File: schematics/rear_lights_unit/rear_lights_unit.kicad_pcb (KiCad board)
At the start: 2 copper layers, 0 parts

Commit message: rear light unit: finished first draft of PCB, regenerated all related files
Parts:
- added BT1: Battery_Cell, FarrhadTech:BatteryHolder_18650, B.Cu at (138.3, 110.5)
- added C1: 0.01uF, Capacitor_THT:C_Rect_L4.6mm_W2.0mm_P2.50mm_MKS02_FKP02, B.Cu at (61.6, 117.9)
- added C2: 10uF, Capacitor_THT:C_Rect_L4.6mm_W2.0mm_P2.50mm_MKS02_FKP02, B.Cu at (72.9, 102.1)
- added C3: 0.01uF, Capacitor_THT:C_Rect_L4.6mm_W2.0mm_P2.50mm_MKS02_FKP02, B.Cu at (94.6, 117.9)
- added C4: 10uF, Capacitor_THT:C_Rect_L4.6mm_W2.0mm_P2.50mm_MKS02_FKP02, B.Cu at (105.9, 102.1)
- added C5: 10uF, Capacitor_THT:CP_Radial_D5.0mm_P2.00mm, B.Cu at (54.6, 96.8)
- added D1: LED, LED_THT:LED_D5.0mm, F.Cu at (104.6, 59.9)
- added D10: LED, LED_THT:LED_D5.0mm, F.Cu at (162.1, 68.1)
- added D11: LED, LED_THT:LED_D5.0mm, F.Cu at (162.1, 76.2)
- added D12: LED, LED_THT:LED_D5.0mm, F.Cu at (162.1, 84.3)
- added D13: LED, LED_THT:LED_D5.0mm, F.Cu at (178.3, 62.2)
- added D14: LED, LED_THT:LED_D5.0mm, F.Cu at (178.3, 71.4)
- added D15: LED, LED_THT:LED_D5.0mm, F.Cu at (178.3, 80.5)
- added D16: LED, LED_THT:LED_D5.0mm, F.Cu at (199.6, 66.8)
- added D17: LED, LED_THT:LED_D5.0mm, F.Cu at (129.0, 60.2)
- added D18: LED, LED_THT:LED_D5.0mm, F.Cu at (129.0, 68.3)
- added D19: LED, LED_THT:LED_D5.0mm, F.Cu at (129.0, 76.5)
- added D2: LED, LED_THT:LED_D5.0mm, F.Cu at (104.6, 68.1)
- added D20: LED, LED_THT:LED_D5.0mm, F.Cu at (129.0, 84.6)
- added D21: LED, LED_THT:LED_D5.0mm, F.Cu at (138.2, 60.2)
- added D22: LED, LED_THT:LED_D5.0mm, F.Cu at (138.2, 68.3)
- added D23: LED, LED_THT:LED_D5.0mm, F.Cu at (138.2, 76.5)
- added D24: LED, LED_THT:LED_D5.0mm, F.Cu at (138.2, 84.6)
- added D25: LED, LED_THT:LED_D5.0mm, F.Cu at (67.0, 77.5)
- added D26: LED, LED_THT:LED_D5.0mm, F.Cu at (199.6, 75.9)
- added D3: LED, LED_THT:LED_D5.0mm, F.Cu at (104.6, 76.2)
- added D4: LED, LED_THT:LED_D5.0mm, F.Cu at (104.6, 84.3)
- added D5: LED, LED_THT:LED_D5.0mm, F.Cu at (88.4, 63.8)
- added D6: LED, LED_THT:LED_D5.0mm, F.Cu at (88.4, 72.9)
- added D7: LED, LED_THT:LED_D5.0mm, F.Cu at (88.4, 82.0)
- added D8: LED, LED_THT:LED_D5.0mm, F.Cu at (67.0, 68.3)
- added D9: LED, LED_THT:LED_D5.0mm, F.Cu at (162.1, 59.9)
- added G***: LOGO, FarrhadTech:resisty_0.5x0.65inch, F.Cu at (155.2, 111.5)
- added J1: Conn_01x04_Socket, Connector_JST:JST_XH_S4B-XH-A_1x04_P2.50mm_Horizontal, B.Cu at (206.0, 84.6)
- added Q1: IRLZ44N, FarrhadTech:TO-220-3_Horizontal_TabUpNoHole, B.Cu at (80.3, 97.3)
- added Q2: IRLZ44N, FarrhadTech:TO-220-3_Horizontal_TabUpNoHole, B.Cu at (113.0, 97.3)
- added R1: 120, Resistor_THT:R_Axial_DIN0207_L6.3mm_D2.5mm_P10.16mm_Horizontal, B.Cu at (101.6, 59.9)
- added R10: 120, Resistor_THT:R_Axial_DIN0207_L6.3mm_D2.5mm_P10.16mm_Horizontal, B.Cu at (165.1, 68.1)
- added R11: 120, Resistor_THT:R_Axial_DIN0207_L6.3mm_D2.5mm_P10.16mm_Horizontal, B.Cu at (165.1, 76.2)
- added R12: 120, Resistor_THT:R_Axial_DIN0207_L6.3mm_D2.5mm_P10.16mm_Horizontal, B.Cu at (165.1, 84.3)
- added R13: 120, Resistor_THT:R_Axial_DIN0207_L6.3mm_D2.5mm_P10.16mm_Horizontal, B.Cu at (183.9, 62.2)
- added R14: 120, Resistor_THT:R_Axial_DIN0207_L6.3mm_D2.5mm_P10.16mm_Horizontal, B.Cu at (183.9, 71.4)
- added R15: 120, Resistor_THT:R_Axial_DIN0207_L6.3mm_D2.5mm_P10.16mm_Horizontal, B.Cu at (183.9, 80.5)
- added R16: 120, Resistor_THT:R_Axial_DIN0207_L6.3mm_D2.5mm_P10.16mm_Horizontal, B.Cu at (202.7, 66.8)
- added R17: 120, Resistor_THT:R_Axial_DIN0207_L6.3mm_D2.5mm_P10.16mm_Horizontal, B.Cu at (126.5, 60.2)
- added R18: 120, Resistor_THT:R_Axial_DIN0207_L6.3mm_D2.5mm_P10.16mm_Horizontal, B.Cu at (126.5, 68.3)
- added R19: 120, Resistor_THT:R_Axial_DIN0207_L6.3mm_D2.5mm_P10.16mm_Horizontal, B.Cu at (126.5, 76.5)
- added R2: 120, Resistor_THT:R_Axial_DIN0207_L6.3mm_D2.5mm_P10.16mm_Horizontal, B.Cu at (101.6, 68.1)
- added R20: 120, Resistor_THT:R_Axial_DIN0207_L6.3mm_D2.5mm_P10.16mm_Horizontal, B.Cu at (126.5, 84.6)
- added R21: 120, Resistor_THT:R_Axial_DIN0207_L6.3mm_D2.5mm_P10.16mm_Horizontal, B.Cu at (150.9, 60.2)
- added R22: 120, Resistor_THT:R_Axial_DIN0207_L6.3mm_D2.5mm_P10.16mm_Horizontal, B.Cu at (150.9, 68.3)
- added R23: 120, Resistor_THT:R_Axial_DIN0207_L6.3mm_D2.5mm_P10.16mm_Horizontal, B.Cu at (150.9, 76.5)
- added R24: 120, Resistor_THT:R_Axial_DIN0207_L6.3mm_D2.5mm_P10.16mm_Horizontal, B.Cu at (150.9, 84.6)
- added R25: 7.5k, Resistor_THT:R_Axial_DIN0207_L6.3mm_D2.5mm_P10.16mm_Horizontal, B.Cu at (72.0, 113.0)
- added R26: 75k, Resistor_THT:R_Axial_DIN0207_L6.3mm_D2.5mm_P10.16mm_Horizontal, B.Cu at (55.4, 113.5)
- added R27: 100, Resistor_THT:R_Axial_DIN0207_L6.3mm_D2.5mm_P10.16mm_Horizontal, B.Cu at (72.6, 108.2)
- added R28: 10k, Resistor_THT:R_Axial_DIN0207_L6.3mm_D2.5mm_P10.16mm_Horizontal, B.Cu at (72.0, 117.9)
- added R29: 7.5k, Resistor_THT:R_Axial_DIN0207_L6.3mm_D2.5mm_P10.16mm_Horizontal, B.Cu at (104.9, 113.0)
- added R3: 120, Resistor_THT:R_Axial_DIN0207_L6.3mm_D2.5mm_P10.16mm_Horizontal, B.Cu at (101.6, 76.2)
- added R30: 75k, Resistor_THT:R_Axial_DIN0207_L6.3mm_D2.5mm_P10.16mm_Horizontal, B.Cu at (88.3, 113.5)
- added R31: 10k, Resistor_THT:R_Axial_DIN0207_L6.3mm_D2.5mm_P10.16mm_Horizontal, B.Cu at (104.9, 117.9)
- added R32: 100, Resistor_THT:R_Axial_DIN0207_L6.3mm_D2.5mm_P10.16mm_Horizontal, B.Cu at (105.7, 108.2)
- added R33: 120, Resistor_THT:R_Axial_DIN0207_L6.3mm_D2.5mm_P10.16mm_Horizontal, B.Cu at (64.0, 77.5)
- added R34: 120, Resistor_THT:R_Axial_DIN0207_L6.3mm_D2.5mm_P10.16mm_Horizontal, B.Cu at (202.7, 75.9)
- added R4: 120, Resistor_THT:R_Axial_DIN0207_L6.3mm_D2.5mm_P10.16mm_Horizontal, B.Cu at (101.6, 84.3)
- added R5: 120, Resistor_THT:R_Axial_DIN0207_L6.3mm_D2.5mm_P10.16mm_Horizontal, B.Cu at (82.8, 63.8)
- added R6: 120, Resistor_THT:R_Axial_DIN0207_L6.3mm_D2.5mm_P10.16mm_Horizontal, B.Cu at (82.8, 72.9)
- added R7: 120, Resistor_THT:R_Axial_DIN0207_L6.3mm_D2.5mm_P10.16mm_Horizontal, B.Cu at (82.8, 82.0)
- added R8: 120, Resistor_THT:R_Axial_DIN0207_L6.3mm_D2.5mm_P10.16mm_Horizontal, B.Cu at (64.0, 68.3)
- added R9: 120, Resistor_THT:R_Axial_DIN0207_L6.3mm_D2.5mm_P10.16mm_Horizontal, B.Cu at (165.1, 59.9)
- added SW2: rocker_switch, Button_Switch_THT:SW_Lever_1P2T_NKK_GW12LxH, B.Cu at (197.9, 90.9)
- added TP1: VBATT, TestPoint:TestPoint_Keystone_5000-5004_Miniature, B.Cu at (184.7, 95.8)
- added TP2: GND, TestPoint:TestPoint_Keystone_5000-5004_Miniature, B.Cu at (168.9, 95.8)
- added TP3: LEFT, TestPoint:TestPoint_Keystone_5000-5004_Miniature, B.Cu at (179.3, 95.8)
- added TP4: RIGHT, TestPoint:TestPoint_Keystone_5000-5004_Miniature, B.Cu at (174.2, 95.8)
- added U1: LMC555xN, Package_DIP:DIP-8_W7.62mm, B.Cu at (66.5, 103.9)
- added U2: LMC555xN, Package_DIP:DIP-8_W7.62mm, B.Cu at (99.6, 103.9)
- added U3: TP4056 module, FarrhadTech:TP4065, B.Cu at (126.8, 104.9)
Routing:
- net V_BATT: track 0.00 -> 474.7 mm
- net GND: track 0.00 -> 360.6 mm
- net Net-(D10-K): track 0.00 -> 205.3 mm
- net LEFT_TURN_EN: track 0.00 -> 200.5 mm
- net RIGHT_TURN_EN: track 0.00 -> 158.2 mm
- net Net-(D1-K): track 0.00 -> 124.8 mm
- net Net-(SW2-A): track 0.00 -> 75.8 mm
- net Net-(BT1--): track 0.00 -> 74.1 mm
- net Net-(BT1-+): track 0.00 -> 34.6 mm
- net Net-(Q2-G): track 0.00 -> 29.3 mm
- net Net-(Q1-G): track 0.00 -> 28.8 mm
- net Net-(U1-DIS): track 0.00 -> 24.7 mm
- net Net-(U2-DIS): track 0.00 -> 24.7 mm
- net Net-(U1-THR): track 0.00 -> 23.4 mm
- net Net-(U2-THR): track 0.00 -> 23.4 mm
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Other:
- board outline added: 163.8 x 71.1 mm
- board text added: "FarrhadTech Rear Light Unit v0"

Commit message: finalized rear light unit v0
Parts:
- removed SW2: rocker_switch, Button_Switch_THT:SW_Lever_1P2T_NKK_GW12LxH
- added REF**: MountingHole_3mm, MountingHole:MountingHole_3mm, F.Cu at (55.6, 54.3)
- added REF**: MountingHole_3mm, MountingHole:MountingHole_3mm, F.Cu at (55.6, 118.4)
- added REF**: MountingHole_3mm, MountingHole:MountingHole_3mm, F.Cu at (212.4, 54.3)
- added SW1: GW12LxH, FarrhadTech:SW_Lever_1P2T_NKK_GW12LxH, B.Cu at (216.9, 87.3)
- U3: footprint FarrhadTech:TP4065 -> FarrhadTech:TP4056_module
- moved U3 15.3 mm to (133.6, 118.6)
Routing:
- net V_BATT: track 474.7 -> 467.3 mm
- net GND: track 360.6 -> 367.3 mm
- net Net-(U3-OUT+): track 75.8 -> 78.5 mm
- net LEFT_TURN_EN: track 200.5 -> 198.2 mm
- net Net-(BT1--): track 74.1 -> 75.9 mm
- net Net-(U1-CV): track 8.61 -> 7.44 mm
- net RIGHT_TURN_EN: track 158.2 -> 159.4 mm
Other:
- board text added: "B+"
- board text added: "B-"

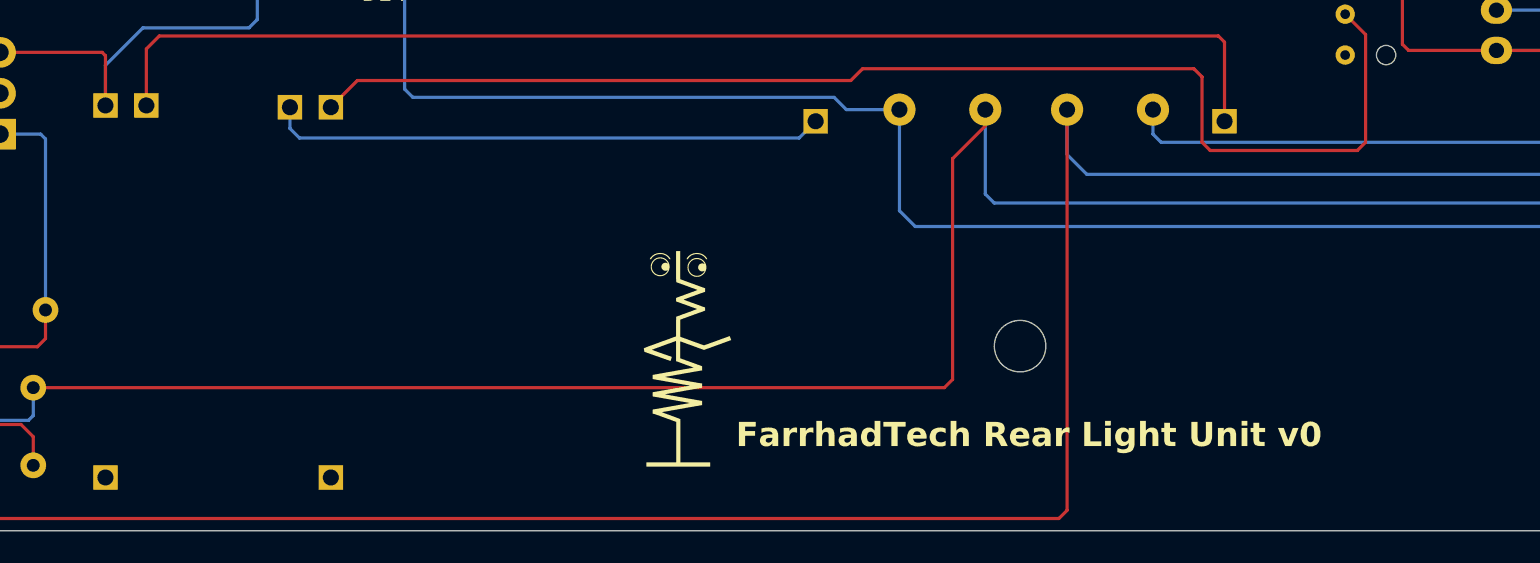
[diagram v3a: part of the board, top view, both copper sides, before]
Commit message: updated both sets of light unit board files to include the newly-added 3D models
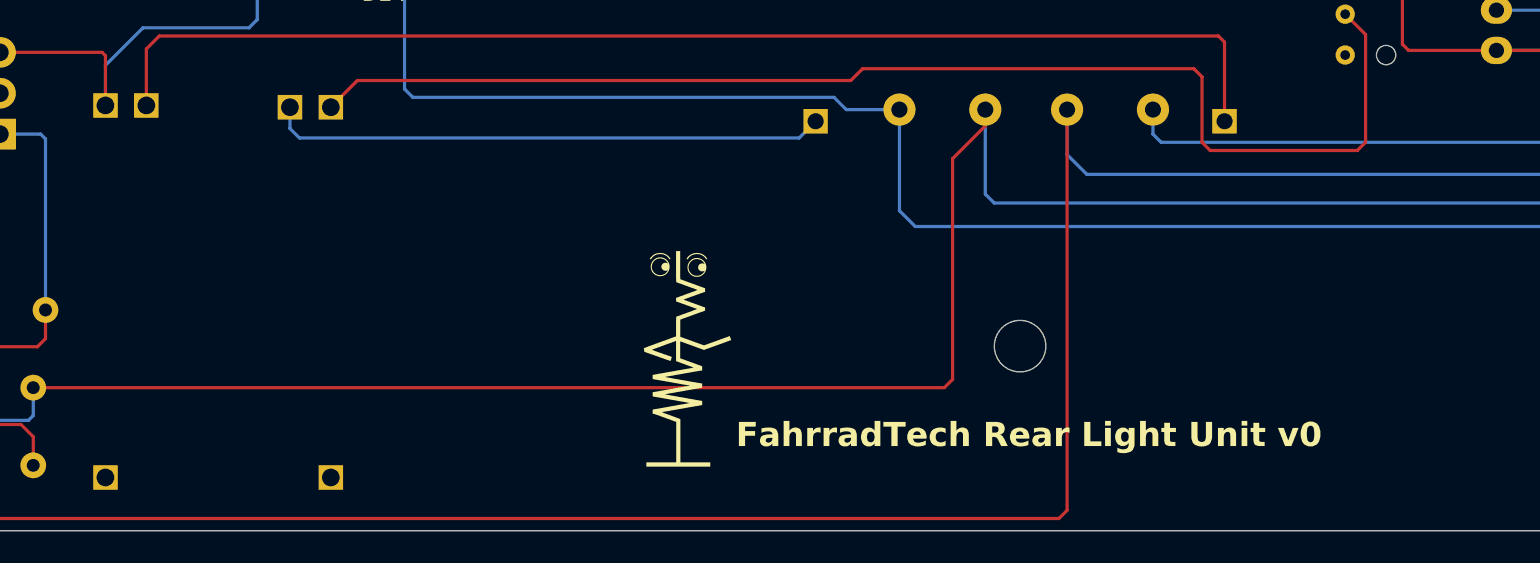
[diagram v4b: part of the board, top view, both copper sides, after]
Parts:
- TP1, TP2, TP3, TP4: footprint TestPoint:TestPoint_Keystone_5000-5004_Miniature -> FahrradTech:TestPoint_Keystone_5000-5004_Miniature
- U3: footprint FarrhadTech:TP4056_module -> FahrradTech:TP4056_module
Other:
- board text added: "FahrradTech Rear Light Unit v0"
- board text removed: "FarrhadTech Rear Light Unit v0"
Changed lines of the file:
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@@
 	(paper "A")
 	(title_block
-		(title "FarrhadTech Rear Lights Unit")
-		(date "2025-03-28")
+		(title "FahrradTech Rear Lights Unit")
+		(date "2025-04-03")
 		(rev "0")
 	)
@@
 			(sketchpadsonfab no)
 			(subtractmaskfromsilk no)
-			(outputformat 1)
+			(outputformat 5)
 			(mirror no)
 			(drillshape 0)
 			(scaleselection 1)
-			(outputdirectory "C:/Users/Katy/source/repos/FarrhadTech/schematics/rear_lights_unit/Gerbers/")
+			(outputdirectory "C:/Users/Katy/source/repos/FarrhadTech/img/")
 		)
 	)
@@
 		)
 	)
-	(footprint "FarrhadTech:TP4056_module"
+	(footprint "FahrradTech:TP4056_module"
 		(layer "B.Cu")
 		(at 133.59 118.61 90)
@@
 			)
 		)
-		(property "Footprint" "FarrhadTech:TP4056_module"
+		(property "Footprint" "FahrradTech:TP4056_module"
 			(at 12.5 -7.1 -90)
 			(unlocked yes)
@@
 			(layer "User.1")
 			(pts
-				(xy 117.99 121.06) (xy 135.19 121.06)
+				(xy 133.59 118.61) (xy 133.58 120.61)
 			)
-			(height 2.57)
-			(orientation 0)
-			(gr_text "17.2000 mm"
-				(at 126.59 122.48 0)
+			(height 2.61)
+			(orientation 1)
+			(gr_text "2.0000 mm"
+				(at 135.05 119.61 90)
 				(layer "User.1")
 				(effects
@@
 			(layer "User.1")
 			(pts
-				(xy 133.59 95.61) (xy 135.19 95.57)
+				(xy 117.99 121.06) (xy 135.19 121.06)
 			)
-			(height 4)
+			(height 2.57)
 			(orientation 0)
-			(gr_text "1.6000 mm"
-				(at 134.39 98.46 0)
+			(gr_text "17.2000 mm"
+				(at 126.59 122.48 0)
 				(layer "User.1")
 				(effects
@@
 			(layer "User.1")
 			(pts
-				(xy 131.05 95.61) (xy 133.59 95.61)
+				(xy 133.59 95.61) (xy 135.19 95.57)
 			)
-			(height -5.45)
+			(height 4)
 			(orientation 0)
-			(gr_text "2.5400 mm"
-				(at 132.32 89.01 0)
+			(gr_text "1.6000 mm"
+				(at 134.39 98.46 0)
 				(layer "User.1")
 				(effects
@@
 			(layer "User.1")
 			(pts
-				(xy 133.59 118.61) (xy 133.58 120.61)
+				(xy 131.05 95.61) (xy 133.59 95.61)
 			)
-			(height 2.61)
-			(orientation 1)
-			(gr_text "2.0000 mm"
-				(at 135.05 119.61 90)
+			(height -5.45)
+			(orientation 0)
+			(gr_text "2.5400 mm"
+				(at 132.32 89.01 0)
 				(layer "User.1")
 				(effects
@@
 			(at 0 0 90)
 			(size 1.524 1.524)
-			(drill 1)
+			(drill 1.1)
 			(layers "*.Cu" "*.Mask")
 			(remove_unused_layers no)
@@
 			(at 0 -14 90)
 			(size 1.524 1.524)
-			(drill 1)
+			(drill 1.1)
 			(layers "*.Cu" "*.Mask")
 			(remove_unused_layers no)
@@
 			(at 23 -2.54 90)
 			(size 1.524 1.524)
-			(drill 1)
+			(drill 1.1)
 			(layers "*.Cu" "*.Mask")
 			(remove_unused_layers no)
@@
 			(at 23.11 -11.46 90)
 			(size 1.524 1.524)
-			(drill 1)
+			(drill 1.1)
 			(layers "*.Cu" "*.Mask")
 			(remove_unused_layers no)
@@
 			(at 23 0 90)
 			(size 1.524 1.524)
-			(drill 1)
+			(drill 1.1)
 			(layers "*.Cu" "*.Mask")
 			(remove_unused_layers no)
@@
 			(at 23.11 -14 90)
 			(size 1.524 1.524)
-			(drill 1)
+			(drill 1.1)
 			(layers "*.Cu" "*.Mask")
 			(remove_unused_layers no)
@@
 			(pintype "power_out")
 		)
+		(model "C:/Users/Katy/source/repos/FahrradTech/schematics/3D_models/TP4056_Charging_Module_Type_C.step"
+			(offset
+				(xyz 12 -7 0)
+			)
+			(scale
+				(xyz 1 1 1)
+			)
+			(rotate
+				(xyz 0 0 180)
+			)
+		)
 	)
 	(footprint "Capacitor_THT:C_Rect_L4.6mm_W2.0mm_P2.50mm_MKS02_FKP02"
@@
 		)
 	)
-	(footprint "TestPoint:TestPoint_Keystone_5000-5004_Miniature"
+	(footprint "FahrradTech:TestPoint_Keystone_5000-5004_Miniature"
 		(layer "B.Cu")
 		(at 184.658 95.758 180)
@@
 			)
 		)
-		(property "Footprint" "TestPoint:TestPoint_Keystone_5000-5004_Miniature"
+		(property "Footprint" "FahrradTech:TestPoint_Keystone_5000-5004_Miniature"
 			(at 0 0 0)
 			(unlocked yes)
@@
 			(pintype "passive")
 		)
-		(model "${KICAD8_3DMODEL_DIR}/TestPoint.3dshapes/TestPoint_Keystone_5000-5004_Miniature.wrl"
+		(model "${KICAD8_3DMODEL_DIR}/TestPoint.3dshapes/TestPoint_Keystone_5005-5009_Compact.step"
 			(offset
 				(xyz 0 0 0)
@@
 		)
 	)
-	(footprint "TestPoint:TestPoint_Keystone_5000-5004_Miniature"
+	(footprint "FahrradTech:TestPoint_Keystone_5000-5004_Miniature"
 		(layer "B.Cu")
 		(at 174.244 95.758 180)
@@
 			)
 		)
-		(property "Footprint" "TestPoint:TestPoint_Keystone_5000-5004_Miniature"
+		(property "Footprint" "FahrradTech:TestPoint_Keystone_5000-5004_Miniature"
 			(at 0 0 0)
 			(unlocked yes)
@@
 			(pintype "passive")
 		)
-		(model "${KICAD8_3DMODEL_DIR}/TestPoint.3dshapes/TestPoint_Keystone_5000-5004_Miniature.wrl"
+		(model "${KICAD8_3DMODEL_DIR}/TestPoint.3dshapes/TestPoint_Keystone_5005-5009_Compact.step"
 			(offset
 				(xyz 0 0 0)
@@
 		)
 	)
-	(footprint "TestPoint:TestPoint_Keystone_5000-5004_Miniature"
+	(footprint "FahrradTech:TestPoint_Keystone_5000-5004_Miniature"
 		(layer "B.Cu")
 		(at 168.91 95.758 180)
@@
 			)
 		)
-		(property "Footprint" "TestPoint:TestPoint_Keystone_5000-5004_Miniature"
+		(property "Footprint" "FahrradTech:TestPoint_Keystone_5000-5004_Miniature"
 			(at 0 0 0)
 			(unlocked yes)
@@
 			(pintype "passive")
 		)
-		(model "${KICAD8_3DMODEL_DIR}/TestPoint.3dshapes/TestPoint_Keystone_5000-5004_Miniature.wrl"
+		(model "${KICAD8_3DMODEL_DIR}/TestPoint.3dshapes/TestPoint_Keystone_5005-5009_Compact.step"
 			(offset
 				(xyz 0 0 0)
@@
 		)
 	)
-	(footprint "TestPoint:TestPoint_Keystone_5000-5004_Miniature"
+	(footprint "FahrradTech:TestPoint_Keystone_5000-5004_Miniature"
 		(layer "B.Cu")
 		(at 179.324 95.758 180)
@@
 			)
 		)
-		(property "Footprint" "TestPoint:TestPoint_Keystone_5000-5004_Miniature"
+		(property "Footprint" "FahrradTech:TestPoint_Keystone_5000-5004_Miniature"
 			(at 0 0 0)
 			(unlocked yes)
@@
 			(pintype "passive")
 		)
-		(model "${KICAD8_3DMODEL_DIR}/TestPoint.3dshapes/TestPoint_Keystone_5000-5004_Miniature.wrl"
+		(model "${KICAD8_3DMODEL_DIR}/TestPoint.3dshapes/TestPoint_Keystone_5005-5009_Compact.step"
 			(offset
 				(xyz 0 0 0)
@@
 		)
 	)
-	(gr_text "FarrhadTech Rear Light Unit v0"
+	(gr_text "FahrradTech Rear Light Unit v0"
 		(at 158.75 116.84 0)
 		(layer "F.SilkS")
